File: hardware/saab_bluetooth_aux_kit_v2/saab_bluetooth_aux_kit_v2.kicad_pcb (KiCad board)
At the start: 2 copper layers, 76.2 x 76.2 mm, 32 parts, among them J2 I2S_MIC, J4 Conn_VCC, J5 Conn_CAN_IBUS, U2 WeMos_LoLin32_Lite, U3 PCM5102_Breakout, U4 UDA1334A, U5 SZMMBZ15VALT3G, U6 VXO7805-500-M-TR, U7 NCP1117LPST33T3G, U9 SN65HVD230

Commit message: V2 Kit looking good!
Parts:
- removed kibuzzard-62F394C5 (x2): G***, kibuzzard-62F394C5
- added J1: Conn_02x08, Connector_PinHeader_2.54mm:PinHeader_2x08_P2.54mm_Vertical, F.Cu at (165.1, 131.2)
- added TP1: CANRX, TestPoint:TestPoint_THTPad_D2.0mm_Drill1.0mm, F.Cu at (179.2, 138.8)
- added TP10: GND, TestPoint:TestPoint_THTPad_D2.0mm_Drill1.0mm, F.Cu at (195.7, 138.8)
- added TP11: GND, TestPoint:TestPoint_THTPad_D2.0mm_Drill1.0mm, F.Cu at (201.2, 180.2)
- added TP2: EN, TestPoint:TestPoint_THTPad_D2.0mm_Drill1.0mm, F.Cu at (205.7, 113.5)
- added TP3: WSEL, TestPoint:TestPoint_THTPad_D2.0mm_Drill1.0mm, F.Cu at (146.2, 122.9)
- added TP4: CANTX, TestPoint:TestPoint_THTPad_D2.0mm_Drill1.0mm, F.Cu at (187.5, 138.8)
- added TP5: DOUT, TestPoint:TestPoint_THTPad_D2.0mm_Drill1.0mm, F.Cu at (148.7, 120.4)
- added TP6: BCK, TestPoint:TestPoint_THTPad_D2.0mm_Drill1.0mm, F.Cu at (151.1, 117.9)
- added TP8: 5V0, TestPoint:TestPoint_THTPad_D2.0mm_Drill1.0mm, F.Cu at (209.8, 165.0)
- added TP9: 3V3, TestPoint:TestPoint_THTPad_D2.0mm_Drill1.0mm, F.Cu at (201.2, 176.9)
- added kibuzzard-632C431C: G***, kibuzzard-632C431C, F.Cu at (174.8, 155.3)
- added kibuzzard-632C431C: G***, kibuzzard-632C431C, B.Cu at (174.8, 155.3)
- added kibuzzard-632C4321: G***, kibuzzard-632C4321, F.Cu at (174.8, 157.4)
- added kibuzzard-632C4321: G***, kibuzzard-632C4321, B.Cu at (174.8, 157.4)
- added kibuzzard-632C4325: G***, kibuzzard-632C4325, F.Cu at (184.9, 155.3)
- added kibuzzard-632C4325: G***, kibuzzard-632C4325, B.Cu at (184.9, 155.3)
- added kibuzzard-632C4329: G***, kibuzzard-632C4329, F.Cu at (184.9, 157.4)
- added kibuzzard-632C4329: G***, kibuzzard-632C4329, B.Cu at (184.9, 157.4)
- added kibuzzard-632C5E36: G***, kibuzzard-632C5E36, F.Cu at (209.3, 137.3)
- added kibuzzard-632C5E36: G***, kibuzzard-632C5E36, B.Cu at (209.3, 137.3)
- added kibuzzard-632C5EA9: G***, kibuzzard-632C5EA9, F.Cu at (166.4, 181.9)
- added kibuzzard-632C5EB0: G***, kibuzzard-632C5EB0, F.Cu at (193.3, 181.9)
- added kibuzzard-632C7032: G***, kibuzzard-632C7032, F.Cu at (164.8, 121.7)
- added kibuzzard-632C7032: G***, kibuzzard-632C7032, B.Cu at (164.8, 121.7)
- moved U5 14.6 mm to (190.0, 156.6), turned to -90 degrees
- moved C1 7.41 mm to (190.0, 152.8)
- moved C2 5.65 mm to (193.3, 146.4), turned to 180 degrees
- moved J2 3.56 mm to (208.0, 128.7), turned to 0 degrees
- moved kibuzzard-62F392E4 2.30 mm to (152.4, 141.9), turned to 0 degrees
- moved U2 1.02 mm to (165.1, 135.0)
- moved C3 0.61 mm to (193.3, 143.9)
- moved U6 0.51 mm to (198.9, 156.1)
- moved kibuzzard-62F3934B 0.38 mm to (155.7, 172.8), turned to 0 degrees
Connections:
- U2 pad 1: unconnected-(U2-Pad1) -> /ESP32/GPIO13
- U2 pad 10: unconnected-(U2-Pad10) -> /ESP32/GPIO23
- U2 pad 12: unconnected-(U2-Pad12) -> /ESP32/GPIO22
- U2 pad 16: unconnected-(U2-Pad16) -> /ESP32/EN
- U2 pad 2: unconnected-(U2-Pad2) -> /ESP32/GPIO15
- U2 pad 3: unconnected-(U2-Pad3) -> /ESP32/GPIO02
- U2 pad 4: unconnected-(U2-Pad4) -> /ESP32/GPIO00
- U2 pad 5: unconnected-(U2-Pad5) -> /ESP32/GPIO04
- U2 pad 6: unconnected-(U2-Pad6) -> /ESP32/GPIO16
- U2 pad 7: unconnected-(U2-Pad7) -> /ESP32/GPIO17
- U2 pad 8: unconnected-(U2-Pad8) -> /ESP32/GPIO05
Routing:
- net I2S0_WSEL: track 0.00 -> 76.9 mm
- net I2S0_DOUT: track 0.00 -> 75.7 mm
- net I2S0_BCK: track 0.00 -> 74.6 mm
- net I2S1_WSEL: track 0.00 -> 56.0 mm
- net I2S1_BCK: track 0.00 -> 47.8 mm
- net I2S1_DIN: track 0.00 -> 36.5 mm
- net CAN_TX: track 0.00 -> 30.9 mm, vias 0 -> 1
- net +12V: track 0.00 -> 23.7 mm, vias 0 -> 1
- net /ESP32/GPIO22: track 0.00 -> 22.4 mm
- net CAN_H: track 0.00 -> 22.1 mm, vias 0 -> 1
- net +5V: track 0.00 -> 21.1 mm
- net CAN_RX: track 0.00 -> 20.6 mm, vias 0 -> 1
- net /ESP32/EN: track 0.00 -> 16.8 mm
- net CAN_L: track 0.00 -> 16.5 mm, vias 0 -> 1
- net Net-(R5-Pad2): track 0.00 -> 16.3 mm, vias 0 -> 2
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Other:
- board text added: "--"
- board text added: "00"
- board text added: "02"
- board text added: "04"
- board text added: "05"
- board text added: "13"
- board text added: "15"
- board text added: "16"
- board text added: "17"
- board text added: "18/CANRX"
- board text added: "19/CANTX"
- board text added: "22"
- board text added: "23"
- board text added: "5V0"
- board text added: "CANRX"
- board text added: "CANTX"
- board text added: "DOUT"
- board text added: "EN"
- board text added: "WSEL"

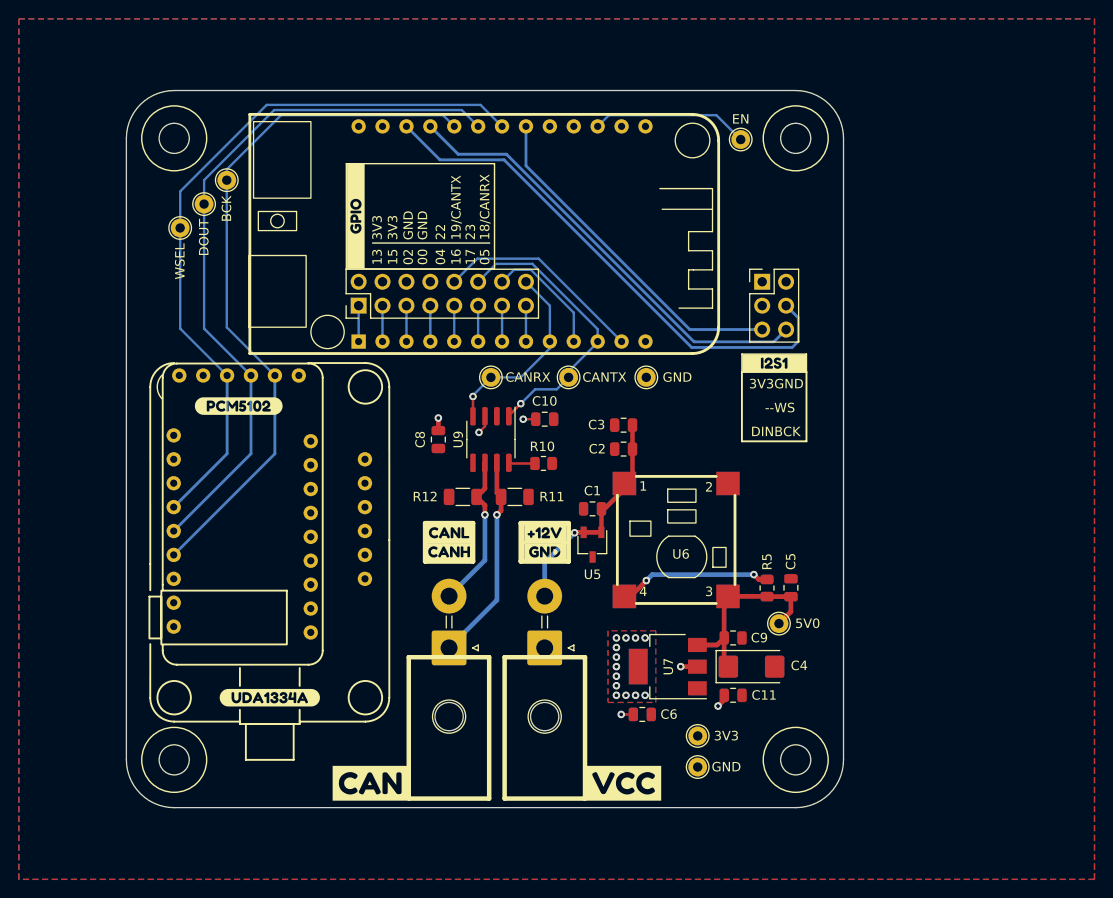
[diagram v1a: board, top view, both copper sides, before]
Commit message: Added bonus power header, which can be used to support additional add-ons in the future
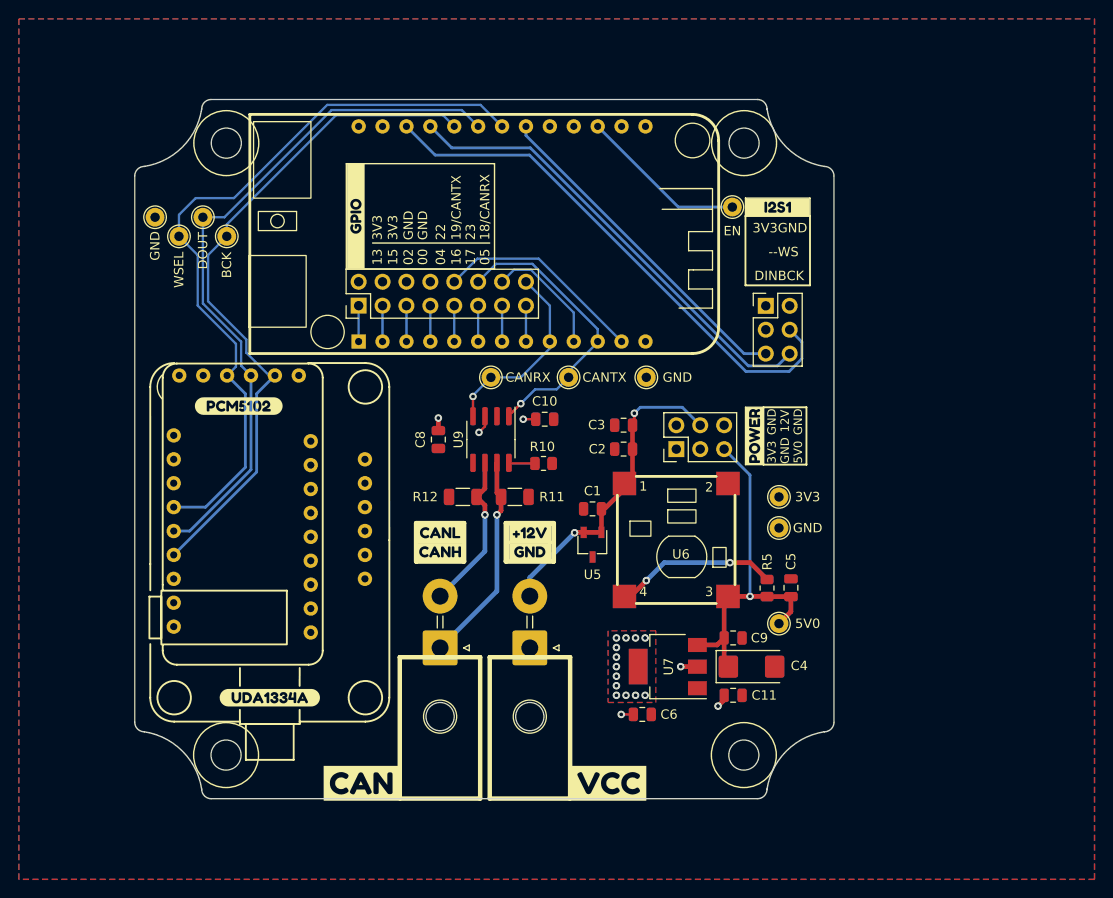
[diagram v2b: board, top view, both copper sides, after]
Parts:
- removed the kibuzzard-632C5E36 at (209.3, 137.3)
- added J3: POWER, Connector_PinHeader_2.54mm:PinHeader_2x03_P2.54mm_Vertical, F.Cu at (198.9, 146.4)
- added TP7: GND, TestPoint:TestPoint_THTPad_D2.0mm_Drill1.0mm, F.Cu at (143.5, 121.8)
- added kibuzzard-632F06BD: G***, kibuzzard-632F06BD, F.Cu at (207.2, 145.0)
- added kibuzzard-632F06BD: G***, kibuzzard-632F06BD, B.Cu at (199.2, 151.6)
- added kibuzzard-632F14FF: G***, kibuzzard-632F14FF, B.Cu at (201.0, 133.7)
- moved TP9 26.8 mm to (209.8, 151.5)
- moved TP11 26.8 mm to (209.8, 154.8)
- moved kibuzzard-632C5E36 16.6 mm to (209.7, 120.7)
- moved TP2 7.23 mm to (204.9, 120.7)
- moved TP6 5.97 mm to (151.1, 123.8)
- moved H3 5.56 mm to (151.1, 113.9)
- moved H1 5.54 mm to (206.1, 178.9)
- moved H4 5.54 mm to (151.1, 178.9)
- moved H2 5.51 mm to (206.1, 113.9)
- moved J2 2.58 mm to (208.4, 131.2)
- moved J4 1.58 mm to (183.3, 167.6)
- moved kibuzzard-632C4325 1.58 mm to (183.3, 155.3) (x2)
- moved kibuzzard-632C4329 1.58 mm to (183.3, 157.4) (x2)
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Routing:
- net +5V: track 21.1 -> 37.8 mm, vias 0 -> 1
- net +12V: track 23.7 -> 33.7 mm, vias 1 -> 2
- net I2S0_WSEL: track 76.9 -> 80.0 mm
- net I2S1_BCK: track 47.8 -> 49.3 mm
- net I2S0_BCK: track 74.6 -> 73.2 mm
- net I2S0_DOUT: track 75.7 -> 74.5 mm
- net /ESP32/EN: track 16.8 -> 17.9 mm
- net Net-(R5-Pad2): track 16.3 -> 17.4 mm
- net I2S1_WSEL: track 56.0 -> 57.0 mm
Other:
- board size 76.2 x 76.2 mm -> 74.3 x 74.3 mm
- board text added: "12V"
- board text added: "LEIGH OLIVER 2022"
- board text added: "SAAB 93NG BT-AUX V2"
